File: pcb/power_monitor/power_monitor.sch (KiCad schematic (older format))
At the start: 8 parts, among them J1 230V AC Input, J2 230V AC Output, J3 RFID, J4 OLED, J5 WS2812, U1 Wemos-D1-mini

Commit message: Fixed power-monitor PCB, to match real-life fixes
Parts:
- added R4: 15K, Resistor_SMD:R_0603_1608Metric_Pad1.05x0.95mm_HandSolder, symbol Device:R_Small
- J1, J2: symbol Connector_Specialized:Screw_Terminal_01x02 -> power_monitor-rescue:Screw_Terminal_01x02-Connector_Specialized
- J3: value RFID -> OLED; symbol Connector_Specialized:Screw_Terminal_01x04 -> power_monitor-rescue:Screw_Terminal_01x04-Connector_Specialized
- J4: value OLED -> RFID; symbol Connector_Specialized:Screw_Terminal_01x04 -> power_monitor-rescue:Screw_Terminal_01x04-Connector_Specialized
- J5: symbol Connector_Specialized:Screw_Terminal_01x03 -> power_monitor-rescue:Screw_Terminal_01x03-Connector_Specialized
- R2, R3: footprint Resistor_SMD:R_0603_1608Metric_Pad0.84x1.00mm_HandSolder -> Resistor_SMD:R_0603_1608Metric_Pad1.05x0.95mm_HandSolder
- U1: symbol MCU_Module:Wemos-D1-mini -> power_monitor-rescue:Wemos-D1-mini-MCU_Module
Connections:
- net GND: now also R4.2
- net RFID_SW: now also R4.1
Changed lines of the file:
@@
 	3425 4350 3675 4350
 $Comp
-L MCU_Module:Wemos-D1-mini U1
+L power_monitor-rescue:Wemos-D1-mini-MCU_Module U1
 U 1 1 5AC90283
 P 6325 4100
@@
 	6700 4400 6700 4475
 $Comp
-L Connector_Specialized:Screw_Terminal_01x02 J2
+L power_monitor-rescue:Screw_Terminal_01x02-Connector_Specialized J2
 U 1 1 5ACA6825
 P 3225 4250
@@
 $EndComp
 $Comp
-L Connector_Specialized:Screw_Terminal_01x02 J1
+L power_monitor-rescue:Screw_Terminal_01x02-Connector_Specialized J1
 U 1 1 5ACA682C
 P 3225 3900
@@
 F 0 "R2" H 5659 3296 50  0000 L CNN
 F 1 "6K8" H 5659 3205 50  0000 L CNN
-F 2 "Resistor_SMD:R_0603_1608Metric_Pad0.84x1.00mm_HandSolder" H 5600 3250 50  0001 C CNN
+F 2 "Resistor_SMD:R_0603_1608Metric_Pad1.05x0.95mm_HandSolder" H 5600 3250 50  0001 C CNN
 F 3 "~" H 5600 3250 50  0001 C CNN
 	1    5600 3250
@@
 F 0 "R3" H 5659 3596 50  0000 L CNN
 F 1 "15K" H 5659 3505 50  0000 L CNN
-F 2 "Resistor_SMD:R_0603_1608Metric_Pad0.84x1.00mm_HandSolder" H 5600 3550 50  0001 C CNN
+F 2 "Resistor_SMD:R_0603_1608Metric_Pad1.05x0.95mm_HandSolder" H 5600 3550 50  0001 C CNN
 F 3 "~" H 5600 3550 50  0001 C CNN
 	1    5600 3550
@@
 	6925 3500 6925 3325
 $Comp
-L Connector_Specialized:Screw_Terminal_01x04 J4
+L power_monitor-rescue:Screw_Terminal_01x04-Connector_Specialized J4
 U 1 1 5ACA4C22
 P 7950 3925
 F 0 "J4" H 8075 3825 50  0000 C CNN
-F 1 "OLED" H 8125 3925 50  0000 C CNN
+F 1 "RFID" H 8125 3925 50  0000 C CNN
 F 2 "Connector_Phoenix_MC:PhoenixContact_MC_1,5_4-G-3.81_1x04_P3.81mm_Horizontal" H 7950 3925 50  0001 C CNN
 F 3 "~" H 7950 3925 50  0001 C CNN
@@
 $EndComp
 $Comp
-L Connector_Specialized:Screw_Terminal_01x03 J5
+L power_monitor-rescue:Screw_Terminal_01x03-Connector_Specialized J5
 U 1 1 5ACA4CDB
 P 7950 4325
@@
 $EndComp
 $Comp
-L Connector_Specialized:Screw_Terminal_01x04 J3
+L power_monitor-rescue:Screw_Terminal_01x04-Connector_Specialized J3
 U 1 1 5ACA4D49
 P 7950 3425
 F 0 "J3" H 8075 3325 50  0000 C CNN
-F 1 "RFID" H 8100 3425 50  0000 C CNN
+F 1 "OLED" H 8100 3425 50  0000 C CNN
 F 2 "Connector_Phoenix_MC:PhoenixContact_MC_1,5_4-G-3.81_1x04_P3.81mm_Horizontal" H 7950 3425 50  0001 C CNN
 F 3 "~" H 7950 3425 50  0001 C CNN
@@
 Wire Wire Line
 	5600 3400 5600 3450
+$Comp
+L Device:R_Small R4
+U 1 1 5BD988D9
+P 5400 4375
+F 0 "R4" H 5459 4421 50  0000 L CNN
+F 1 "15K" H 5459 4330 50  0000 L CNN
+F 2 "Resistor_SMD:R_0603_1608Metric_Pad1.05x0.95mm_HandSolder" H 5400 4375 50  0001 C CNN
+F 3 "~" H 5400 4375 50  0001 C CNN
+	1    5400 4375
+	-1   0    0    -1
+$EndComp
+$Comp
+L power:GND #PWR0111
+U 1 1 5BD98B30
+P 5400 4475
+F 0 "#PWR0111" H 5400 4225 50  0001 C CNN
+F 1 "GND" H 5405 4302 50  0000 C CNN
+F 2 "" H 5400 4475 50  0001 C CNN
+F 3 "" H 5400 4475 50  0001 C CNN
+	1    5400 4475
+	1    0    0    -1
+$EndComp
+Text GLabel 5400 4275 1    50   Input ~ 0
+RFID_SW
 $EndSCHEMATC

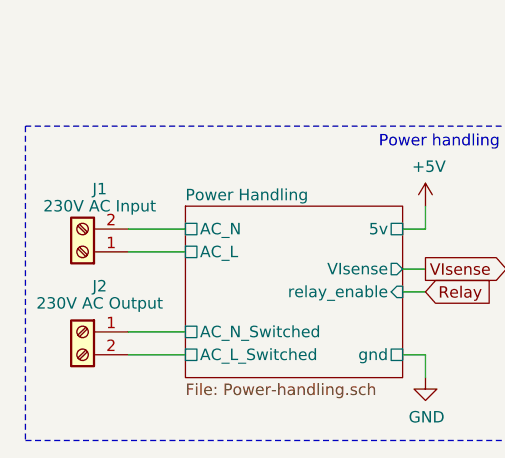
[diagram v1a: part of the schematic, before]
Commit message: Updated power_monitor pcb to use IRM-02 PSU
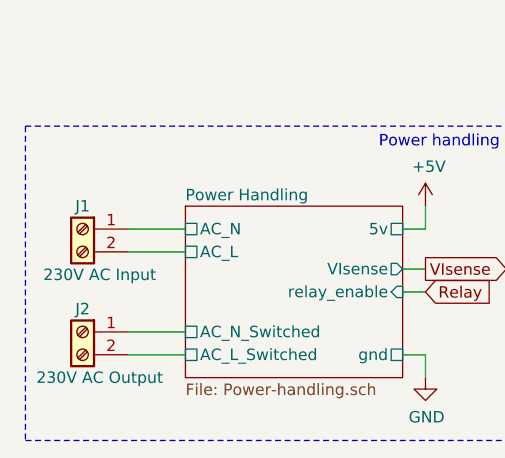
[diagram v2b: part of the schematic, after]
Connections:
- net Power Handling/AC_L: now also J1.2 (Pin_2); no longer J1.1 (Pin_1)
- net Power Handling/AC_N: now also J1.1 (Pin_1); no longer J1.2 (Pin_2)
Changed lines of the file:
@@
 U 1 1 5ACA6825
 P 3225 4250
-F 0 "J2" H 3150 4450 50  0000 C CNN
-F 1 "230V AC Output" H 3150 4375 50  0000 C CNN
+F 0 "J2" H 3225 4350 50  0000 C CNN
+F 1 "230V AC Output" H 3150 4050 50  0000 C CNN
 F 2 "Connector_Phoenix_MSTB:PhoenixContact_MSTBA_2,5_2-G_1x02_P5.00mm_Horizontal" H 3225 4250 50  0001 C CNN
 F 3 "~" H 3225 4250 50  0001 C CNN
@@
 L power_monitor-rescue:Screw_Terminal_01x02-Connector_Specialized J1
 U 1 1 5ACA682C
-P 3225 3900
-F 0 "J1" H 3150 3625 50  0000 C CNN
-F 1 "230V AC Input" H 3150 3700 50  0000 C CNN
-F 2 "Connector_Phoenix_MSTB:PhoenixContact_MSTBA_2,5_2-G_1x02_P5.00mm_Horizontal" H 3225 3900 50  0001 C CNN
-F 3 "~" H 3225 3900 50  0001 C CNN
-	1    3225 3900
-	-1   0    0    1
+P 3225 3800
+F 0 "J1" H 3225 3900 50  0000 C CNN
+F 1 "230V AC Input" H 3150 3600 50  0000 C CNN
+F 2 "Connector_Phoenix_MSTB:PhoenixContact_MSTBA_2,5_2-G_1x02_P5.00mm_Horizontal" H 3225 3800 50  0001 C CNN
+F 3 "~" H 3225 3800 50  0001 C CNN
+	1    3225 3800
+	-1   0    0    -1
 $EndComp
 $Comp
